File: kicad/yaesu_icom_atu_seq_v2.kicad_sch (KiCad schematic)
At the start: 124 parts, among them J1 ICOM ATU, J10 SERIAL, J11 PGLINK, J12 POWER, J13 Icom ATU, J14 I2C, J15 ALC OUT, J16 SEQ A1-3, J17 SEQ B1-3, J18 SEQ C1-3, J19 SEQ D1-3, J2 STBY, J20 SERIAL, J3 TUNER, J4 POWER, J5 I2C, J6 ALC, J7 STBY, J8 TUNER, J9 PVLINK, SW1 TUNE, U1 PC817, U10 PC817, U11 PC817, U12 PC817, U13 PC817, U14 PC817, U15 PC817, U16 PC817, U17 MAX202CPE, U2 L7805, U3 PC817, U4 PC817, U5 PC817, U6 PC817, U7 PC817, U8 PC817, U9 PC817

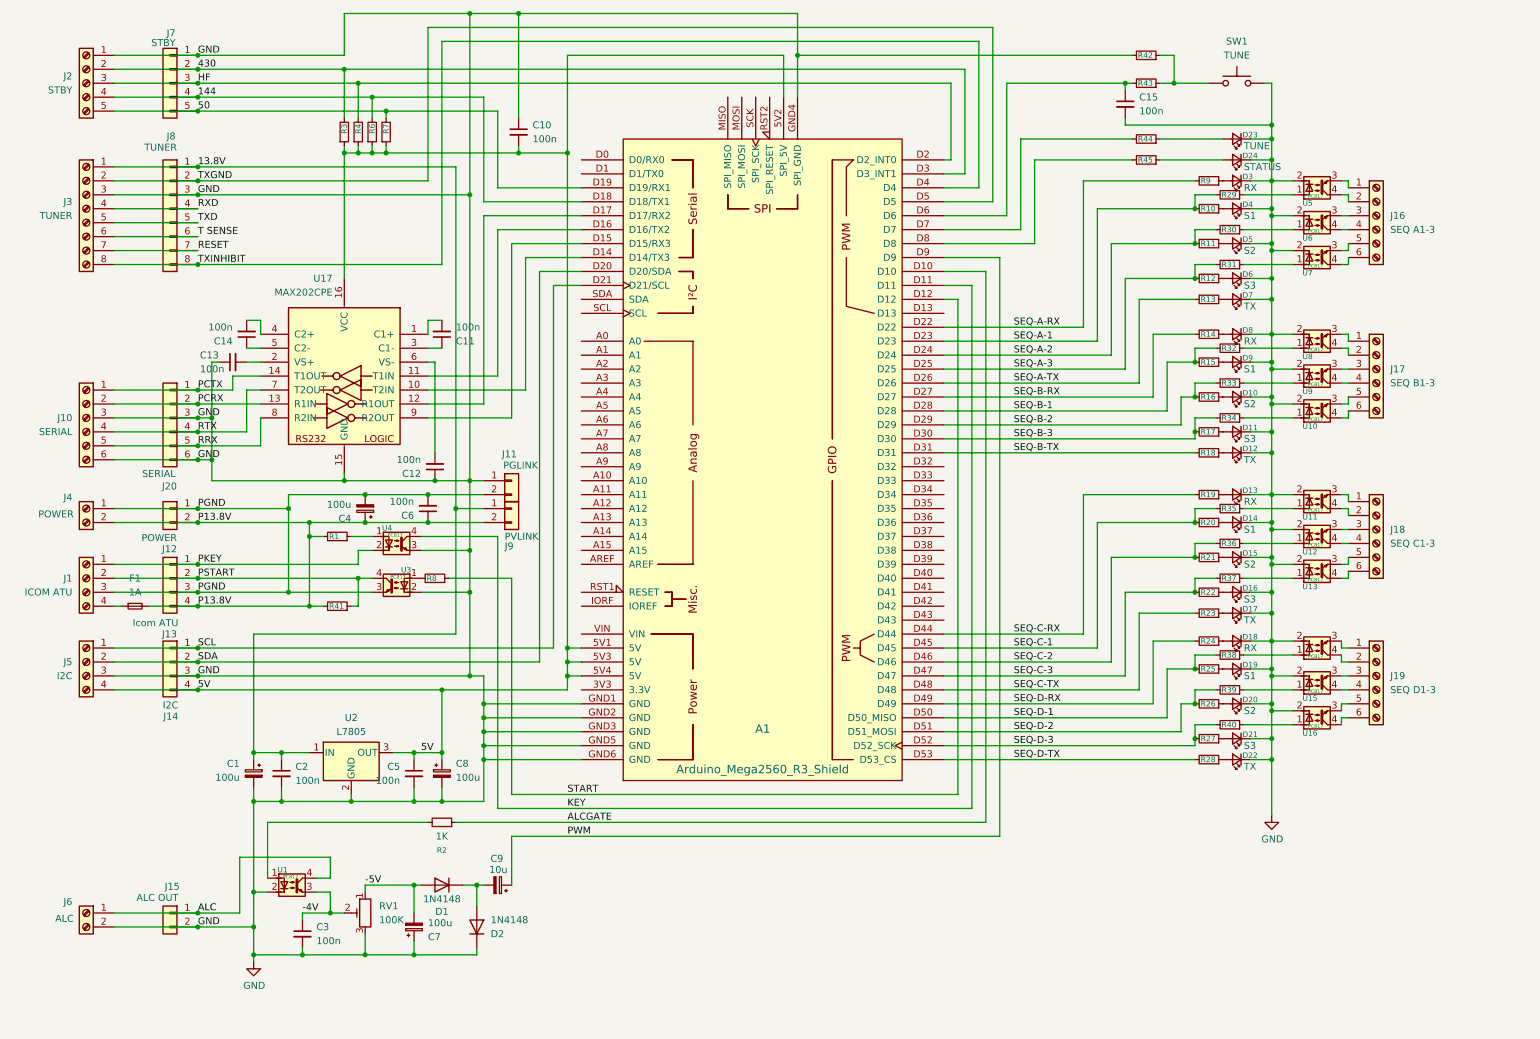
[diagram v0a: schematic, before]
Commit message: update schematic
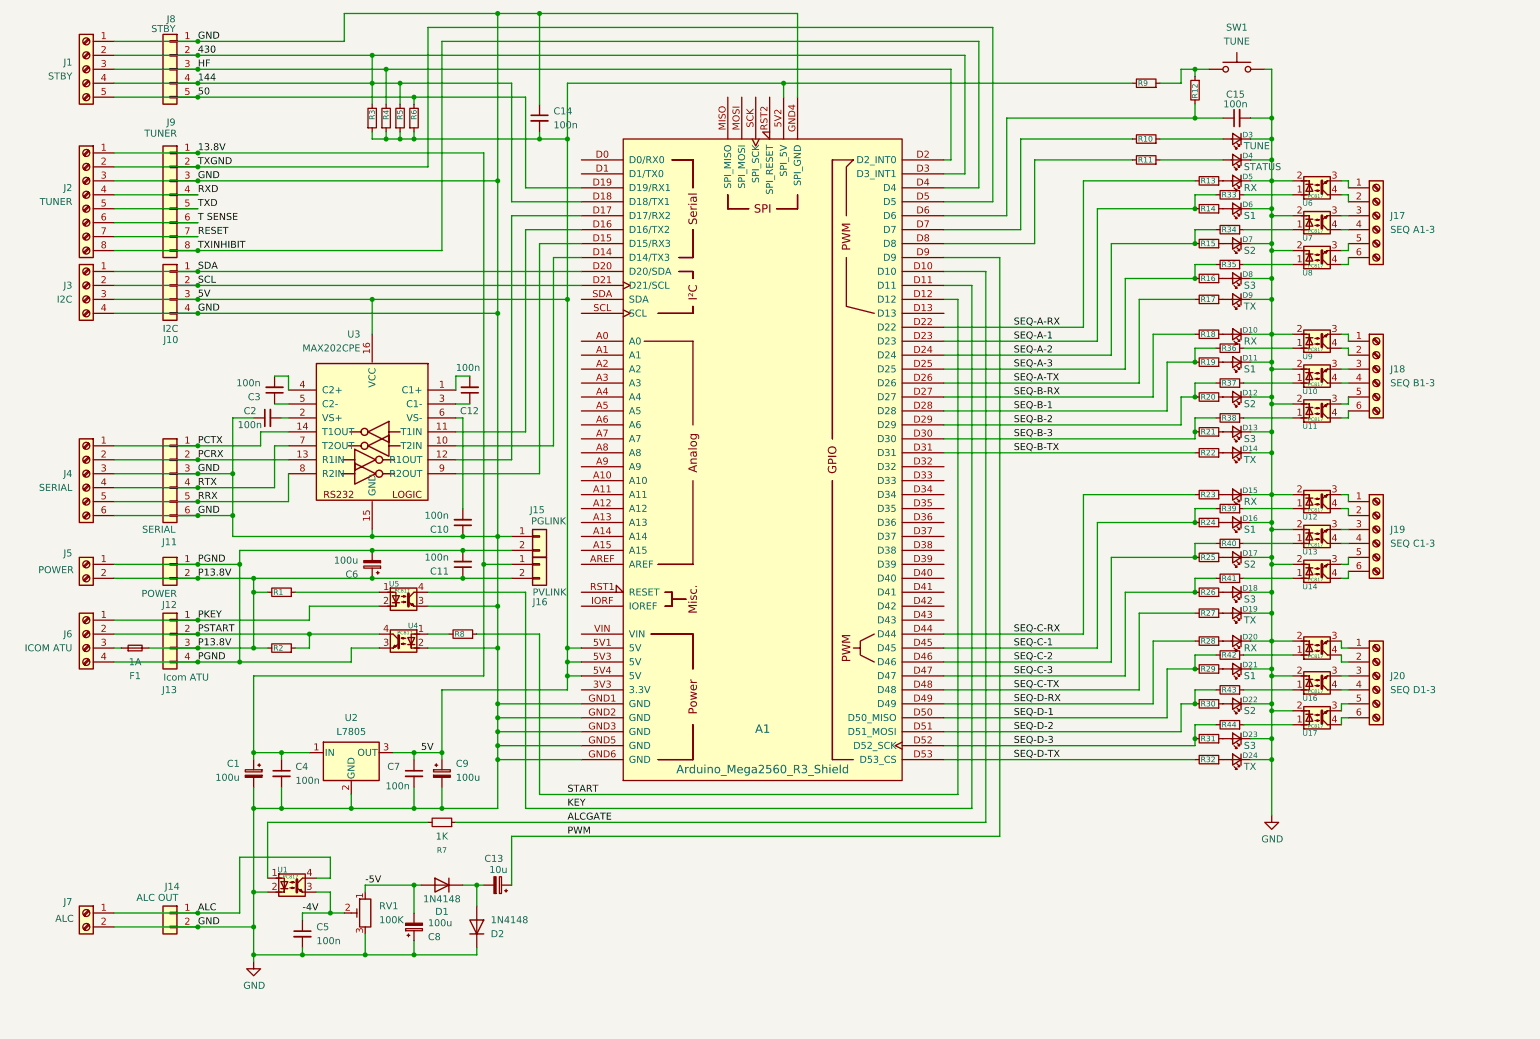
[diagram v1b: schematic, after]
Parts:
- renumbered C12 to C10, C6 to C11, C11 to C12, C9 to C13, C10 to C14, C13 to C2, C14 to C3, C2 to C4, C3 to C5, C4 to C6, C5 to C7, C7 to C8, C8 to C9, D8 to D10, D9 to D11, D10 to D12, D11 to D13, D12 to D14, D13 to D15, D14 to D16, D15 to D17, D16 to D18, D17 to D19, D18 to D20, D19 to D21, D20 to D22, D21 to D23, D22 to D24, D23 to D3, D24 to D4, D3 to D5, D4 to D6, D5 to D7, D6 to D8, D7 to D9, J2 to J1, J14 to J10, J20 to J11, J15 to J14, J11 to J15, J9 to J16, J16 to J17, J17 to J18, J18 to J19, J3 to J2, J19 to J20, J5 to J3, J10 to J4, J4 to J5, J1 to J6, J6 to J7, J7 to J8, J8 to J9, R44 to R10, R45 to R11, R43 to R12, R9 to R13, R10 to R14, R11 to R15, R12 to R16, R13 to R17, R14 to R18, R15 to R19, R41 to R2, R16 to R20, R17 to R21, R18 to R22, R19 to R23, R20 to R24, R21 to R25, R22 to R26, R23 to R27, R24 to R28, R25 to R29, R26 to R30, R27 to R31, R28 to R32, R29 to R33, R30 to R34, R31 to R35, R32 to R36, R33 to R37, R34 to R38, R35 to R39, R36 to R40, R37 to R41, R38 to R42, R39 to R43, R40 to R44, R6 to R5, R7 to R6, R2 to R7, R42 to R9, U9 to U10, U10 to U11, U11 to U12, U12 to U13, U13 to U14, U14 to U15, U15 to U16, U16 to U17, U17 to U3, U3 to U4, U4 to U5, U5 to U6, U6 to U7, U7 to U8, U8 to U9
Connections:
- net 430 is gone; now on net 144: A1.D3 (D3_INT1), J1.2 (Pin_2), J8.2 (Pin_2), R3.2
- net 5V: now also J10.3 (Pin_3), J3.3 (Pin_3), R9.2; no longer J10.4 (Pin_4), J3.4 (Pin_4)
- net GND: now also J10.4 (Pin_4), J3.4 (Pin_4); no longer J10.3 (Pin_3), J3.3 (Pin_3), R9.2
- net P13.8V: now also J13.3 (Pin_3); no longer J13.4 (Pin_4)
- net PGND: now also J13.4 (Pin_4), J6.4 (Pin_4); no longer J13.3 (Pin_3), J6.3 (Pin_3)
- net SCL: now also J10.2 (Pin_2), J3.2 (Pin_2); no longer J10.1 (Pin_1), J3.1 (Pin_1)
- net SDA: now also J10.1 (Pin_1), J3.1 (Pin_1); no longer J10.2 (Pin_2), J3.2 (Pin_2)
- net at F1.1: now also J6.3 (Pin_3); no longer J6.4 (Pin_4)
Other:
- moved on the sheet: C10, C11, C12, C14, C15, C2, C3, C6, F1, J1, J10, J11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

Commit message: Update schematic and PCB
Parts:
- removed D3: TUNE, Custom:LED_THT_L72CB_Kingbright, symbol Device:LED_Small
- removed U1, U10, U11, U12, U13, U14, U15, U16, U17, U4, U5, U6, U7, U8, U9: PC817, Custom:PC817_DIP, symbol Misc_Custom:PC817_small
- added BZ1: Buzzer, Buzzer_Beeper:Buzzer_TDK_PS1240P02BT_D12.2mm_H6.5mm, symbol Device:Buzzer
- added C11, C12, C13, C15, C3, C7, C8, C9: 10n, Capacitor_THT:C_Disc_D4.3mm_W1.9mm_P5.00mm, symbol Device:C_Small
- added C25, C26, C27, C28, C29, C30, C31, C32, C33, C34, C35, C36: 10nF, Capacitor_THT:C_Disc_D5.1mm_W3.2mm_P5.00mm, symbol Custom:C_Smaller
- added C6: 100n, Capacitor_THT:C_Disc_D4.3mm_W1.9mm_P5.00mm, symbol Device:C_Small
- added D1, D2, D28, D29, D30, D31, D32, D33, D34, D35, D36, D37, D38, D39: 1.5KE18A, Diode_THT:D_DO-201AE_P15.24mm_Horizontal, symbol Custom:D_TVS_U_Small
- added D27, D3: 1N4148, Diode_THT:D_DO-35_SOD27_P7.62mm_Horizontal, symbol Diode:1N4148
- added E1: (no value), Custom:Hammond_Enclosure_RM2095L, symbol Custom:Enclosure
- added J10: P13.8V, Connector_PinHeader_2.54mm:PinHeader_2x02_P2.54mm_Vertical, symbol Connector_Generic:Conn_02x02_Counter_Clockwise
- added J11, J19: SPARE, Connector_PinHeader_2.54mm:PinHeader_1x05_P2.54mm_Vertical, symbol Connector_Generic:Conn_01x05
- added J20: RVLINK, Connector_PinHeader_2.54mm:PinHeader_1x02_P2.54mm_Vertical, symbol Connector_Generic:Conn_01x02
- added J23, J24: ANALOG, Connector_PinHeader_2.54mm:PinHeader_1x04_P2.54mm_Vertical, symbol Connector_Generic:Conn_01x04
- added J25: EXP, Connector_PinHeader_2.54mm:PinHeader_1x16_P2.54mm_Vertical, symbol Connector:Conn_01x16_Pin
- added J7: SPARE, TerminalBlock_Phoenix:TerminalBlock_Phoenix_PT-1,5-5-3.5-H_1x05_P3.50mm_Horizontal, symbol Connector:Screw_Terminal_01x05
- added J9: PGND, Connector_PinHeader_2.54mm:PinHeader_2x02_P2.54mm_Vertical, symbol Connector_Generic:Conn_02x02_Counter_Clockwise
- added L1, L2, L3, L4: 100uH, Inductor_THT:L_Axial_L9.5mm_D4.0mm_P5.08mm_Vertical_Fastron_SMCC, symbol Device:L_Small
- added PR1, PR2, PR3, PR4, PR5: (no value), Custom:Prototype Area 5x13 with 4 rails (5x17) 2.54mm Grid, symbol Custom:Prototype_Area
- added Q1: BC547, Package_TO_SOT_THT:TO-92L_Wide, symbol Transistor_BJT:BC547
- added R1, R14, R15, R2, R3, R4, R5, R53, R54, R55, R56, R57, R58, R59, R6, R60, R61, R62, R63, R64: 1K, Resistor_THT:R_Axial_DIN0207_L6.3mm_D2.5mm_P10.16mm_Horizontal, symbol Device:R_Small
- added U1, U4, U5, U6, U7: PC817, Custom:3 x PC817 on a DIP-16_W7.62mm_Socket_LongPads, symbol Misc_Custom:PC817_smallx3
- C1, C2: KiLib_Generator (none) -> capacitor/THT/other
- C10: renamed from C5; KiLib_Generator (none) -> capacitor/THT/other
- C14: renamed from C6; KiLib_Generator (none) -> capacitor/THT/other
- C16: renamed from C7; KiLib_Generator (none) -> capacitor/THT/other
- C17: renamed from C8; value 100u -> 10u; KiLib_Generator (none) -> capacitor/THT/other
- C18: renamed from C9; KiLib_Generator (none) -> capacitor/THT/other
- C19: renamed from C12; KiLib_Generator (none) -> capacitor/THT/other
- C20: renamed from C10; KiLib_Generator (none) -> capacitor/THT/other
- C21: renamed from C11; KiLib_Generator (none) -> capacitor/THT/other
- C22: renamed from C13; value 10u -> 4u7; KiLib_Generator (none) -> capacitor/THT/other
- C23: renamed from C14; KiLib_Generator (none) -> capacitor/THT/other
- C24: renamed from C15; KiLib_Generator (none) -> capacitor/THT/other
- C4: renamed from C3; KiLib_Generator (none) -> capacitor/THT/other
- C5: renamed from C4; KiLib_Generator (none) -> capacitor/THT/other
- D10: renamed from D8; KiLib_Generator (none) -> LED/THT
- D11: renamed from D9; KiLib_Generator (none) -> LED/THT
- D12: renamed from D10; KiLib_Generator (none) -> LED/THT
- D13: renamed from D11; KiLib_Generator (none) -> LED/THT
- D14: renamed from D12; KiLib_Generator (none) -> LED/THT
- D15: renamed from D13; KiLib_Generator (none) -> LED/THT
- D16: renamed from D14; KiLib_Generator (none) -> LED/THT
- D17: renamed from D15; KiLib_Generator (none) -> LED/THT
- D18: renamed from D16; KiLib_Generator (none) -> LED/THT
- D19: renamed from D17; KiLib_Generator (none) -> LED/THT
- D20: renamed from D18; KiLib_Generator (none) -> LED/THT
- D21: renamed from D19; KiLib_Generator (none) -> LED/THT
- D22: renamed from D20; KiLib_Generator (none) -> LED/THT
- D23: renamed from D21; KiLib_Generator (none) -> LED/THT
- D24: renamed from D22; KiLib_Generator (none) -> LED/THT
- D25: renamed from D23; KiLib_Generator (none) -> LED/THT
- D26: renamed from D24; KiLib_Generator (none) -> LED/THT
- D4: renamed from D1; KiLib_Generator (none) -> diode/THT
- D5: renamed from D2; KiLib_Generator (none) -> diode/THT
- D6: renamed from D4; KiLib_Generator (none) -> LED/THT
- D7: renamed from D5; KiLib_Generator (none) -> LED/THT
- D8: renamed from D6; KiLib_Generator (none) -> LED/THT
- D9: renamed from D7; KiLib_Generator (none) -> LED/THT
- J1, J2, J3, J4, J5, J6: KiLib_Generator (none) -> terminal_block/Phoenix
- J12: renamed from J8; KiLib_Generator (none) -> connector/pin_header_socket
- J13: renamed from J9; KiLib_Generator (none) -> connector/pin_header_socket
- J14: renamed from J10; KiLib_Generator (none) -> connector/pin_header_socket
- J15: renamed from J11; KiLib_Generator (none) -> connector/pin_header_socket
- J16: renamed from J12; KiLib_Generator (none) -> connector/pin_header_socket
- J17: renamed from J13; KiLib_Generator (none) -> connector/pin_header_socket
- J18: renamed from J14; KiLib_Generator (none) -> connector/pin_header_socket
- J21: renamed from J15; KiLib_Generator (none) -> connector/pin_header_socket
- J22: renamed from J16; KiLib_Generator (none) -> connector/pin_header_socket
- J26: renamed from J17; KiLib_Generator (none) -> terminal_block/Phoenix
- J27: renamed from J18; KiLib_Generator (none) -> terminal_block/Phoenix
- J28: renamed from J19; KiLib_Generator (none) -> terminal_block/Phoenix
- J29: renamed from J20; KiLib_Generator (none) -> terminal_block/Phoenix
- J8: renamed from J7; KiLib_Generator (none) -> terminal_block/Phoenix
- R10: renamed from R4; KiLib_Generator (none) -> resistor/THT
- R11: renamed from R5; KiLib_Generator (none) -> resistor/THT
- R12: renamed from R6; KiLib_Generator (none) -> resistor/THT
- R13: renamed from R7; value 1K -> 470R; KiLib_Generator (none) -> resistor/THT
- R16: renamed from R8; KiLib_Generator (none) -> resistor/THT
- R17: renamed from R9; KiLib_Generator (none) -> resistor/THT
- R18: renamed from R10; value 1K -> 390R; KiLib_Generator (none) -> resistor/THT
- R19: renamed from R11; KiLib_Generator (none) -> resistor/THT
- R20: renamed from R12; KiLib_Generator (none) -> resistor/THT
- R21: renamed from R13; KiLib_Generator (none) -> resistor/THT
- R22: renamed from R14; KiLib_Generator (none) -> resistor/THT
- R23: renamed from R15; KiLib_Generator (none) -> resistor/THT
- R24: renamed from R16; KiLib_Generator (none) -> resistor/THT
- R25: renamed from R17; KiLib_Generator (none) -> resistor/THT
- R26: renamed from R18; KiLib_Generator (none) -> resistor/THT
- R27: renamed from R19; KiLib_Generator (none) -> resistor/THT
- R28: renamed from R20; KiLib_Generator (none) -> resistor/THT
- R29: renamed from R21; KiLib_Generator (none) -> resistor/THT
- R30: renamed from R22; KiLib_Generator (none) -> resistor/THT
- R31: renamed from R23; KiLib_Generator (none) -> resistor/THT
- R32: renamed from R24; KiLib_Generator (none) -> resistor/THT
- R33: renamed from R25; KiLib_Generator (none) -> resistor/THT
- R34: renamed from R26; KiLib_Generator (none) -> resistor/THT
- R35: renamed from R27; KiLib_Generator (none) -> resistor/THT
- R36: renamed from R28; KiLib_Generator (none) -> resistor/THT
- R37: renamed from R29; KiLib_Generator (none) -> resistor/THT
- R38: renamed from R30; KiLib_Generator (none) -> resistor/THT
- R39: renamed from R31; KiLib_Generator (none) -> resistor/THT
- R40: renamed from R32; KiLib_Generator (none) -> resistor/THT
- R41: renamed from R33; KiLib_Generator (none) -> resistor/THT
- R42: renamed from R34; KiLib_Generator (none) -> resistor/THT
- R43: renamed from R35; KiLib_Generator (none) -> resistor/THT
- R44: renamed from R36; KiLib_Generator (none) -> resistor/THT
- R45: renamed from R37; KiLib_Generator (none) -> resistor/THT
- R46: renamed from R38; KiLib_Generator (none) -> resistor/THT
- R47: renamed from R39; KiLib_Generator (none) -> resistor/THT
- R48: renamed from R40; KiLib_Generator (none) -> resistor/THT
- R49: renamed from R41; KiLib_Generator (none) -> resistor/THT
- R50: renamed from R42; KiLib_Generator (none) -> resistor/THT
- R51: renamed from R43; KiLib_Generator (none) -> resistor/THT
- R52: renamed from R44; KiLib_Generator (none) -> resistor/THT
- R7: renamed from R1; KiLib_Generator (none) -> resistor/THT
- R8: renamed from R2; KiLib_Generator (none) -> resistor/THT
- R9: renamed from R3; KiLib_Generator (none) -> resistor/THT
- SW1: footprint Package_DIP:DIP-24_W7.62mm -> Button_Switch_THT:SW_PUSH-12mm
- U2: KiLib_Generator (none) -> package/TO_SOT/THT
- U3: footprint (none) -> Package_DIP:DIP-16_W7.62mm_Socket_LongPads; KiLib_Generator (none) -> package/DIP/legacy
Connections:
- net -4V: now also U1.9
- net 13.8V: now also J20.2 (Pin_2), J25.1 (Pin_1), PR1.3 (VDD), PR2.3 (VDD), PR3.3 (VDD), PR4.3 (VDD), PR5.3 (VDD), R14.1; no longer J13.1 (Pin_1), J2.1 (Pin_1)
- net 144: now also R3.2; no longer A1.D18 (D18/TX1), A1.D3 (D3_INT1), J1.2 (Pin_2), J12.2 (Pin_2), R11.2, R9.2
- net 50: now also R4.2; no longer A1.D19 (D19/RX1), R12.2
- net 5V: now also J25.2 (Pin_2), PR1.2 (VCC), PR2.2 (VCC), PR3.2 (VCC), PR4.2 (VCC), PR5.2 (VCC)
- net ALC: now also C6.1, U1.10
- net GND: now also BZ1.2 (-), C12.2, C13.2, C3.2, C6.2, C7.2, C8.2, C9.1, D27.2 (A), J25.3 (Pin_3), PR1.1 (GND), PR1.4 (GND), PR2.1 (GND), PR2.4 (GND), PR3.1 (GND), PR3.4 (GND), PR4.1 (GND), PR4.4 (GND), PR5.1 (GND), PR5.4 (GND), Q1.3 (E), U1.15, U1.5, U1.8, U4.2, U4.5, U4.8, U5.2, U5.5, U5.8, U6.2, U6.5, U6.8, U7.2, U7.5, U7.8
- net HF: now also R2.2; no longer A1.D2 (D2_INT0), R10.2
- net KEY: now also U1.16
- net P13.8V: now also J10.1 (Pin_1), J10.2 (Pin_2), J10.3 (Pin_3), J10.4 (Pin_4); no longer J17.3 (Pin_3)
- net PGND: now also C11.2, C15.2, D1.2 (A2), D2.2 (A2), J9.1 (Pin_1), J9.2 (Pin_2), J9.3 (Pin_3), J9.4 (Pin_4), U1.12
- net PKEY: now also D2.1 (A1), L2.1
- net PSTART: now also D1.1 (A1), L1.1; no longer R8.1
- net PWM: now also R15.1; no longer C22.1
- net SEQ-A-1: now also A1.D35; no longer A1.D23
- net SEQ-A-2: now also A1.D36; no longer A1.D24
- net SEQ-A-3: now also A1.D37; no longer A1.D25
- net SEQ-A-RX: now also A1.D34; no longer A1.D22
- net SEQ-A-TX: now also A1.D38; no longer A1.D26
- net SEQ-B-1: now also A1.D40; no longer A1.D28
- net SEQ-B-2: now also A1.D41; no longer A1.D29
- net SEQ-B-3: now also A1.D42; no longer A1.D30
- net SEQ-B-RX: now also A1.D39; no longer A1.D27
- net SEQ-B-TX: now also A1.D43; no longer A1.D31
- net START: now also R16.2, U1.4; no longer A1.D12, R16.1
- net TXGND: now also R5.2; no longer A1.D5
- net TXINHIBIT: now also R6.2; no longer A1.D4
- net at R45.1: now also U5.4
- net at J27.3 (Pin_3): now also C29.2, D29.1 (A1), R57.1
- net at J27.4 (Pin_4): now also C29.1, D29.2 (A2), U5.12
- net ND18: now reaches D18.2 (A), R32.1
- net ND18: now also U6.11, U6.6
- net at R7.1: now also U1.1
- net at A1.A12: now also J24.1 (Pin_1)
- net at A1.A13: now also J24.2 (Pin_2)
- net at A1.A14: now also J24.3 (Pin_3)
- net at A1.A15: now also J24.4 (Pin_4)
- net at A1.A4: now also J23.1 (Pin_1)
- net at A1.A5: now also J23.2 (Pin_2)
- net at A1.A6: now also J23.3 (Pin_3)
- net at A1.A7: now also J23.4 (Pin_4)
- net D13: now reaches A1.D13
- net D13: now also J25.4 (Pin_4)
- net D32: now reaches A1.D32
- net D32: now also J25.15 (Pin_15)
- net D33: now reaches A1.D33
- net D33: now also J25.16 (Pin_16)
- net at A1.D6, C24.1: now also R20.1; no longer R20.2
- net at R46.1: now also U5.1
- net at J26.1 (Pin_1): now also C25.2, D31.1 (A1), R53.1
- net at J26.2 (Pin_2): now also C25.1, D31.2 (A2), U4.9
- net at J26.3 (Pin_3): now also C26.2, D32.1 (A1), R54.1
- net at J26.4 (Pin_4): now also C26.1, D32.2 (A2), U4.12
- net at J26.5 (Pin_5): now also C27.2, D33.1 (A1), R55.1
- net at J26.6 (Pin_6): now also C27.1, D33.2 (A2), U4.15
- net at R13.2: now also U1.7
- net at R41.1: now also U4.7
- net ND14: now reaches D14.2 (A), R28.1
- net ND14: now also U5.14, U5.3
- net at R50.1: now also U7.7
- net at R52.1: now also U7.1
- net at J29.5 (Pin_5): now also C36.2, D39.1 (A1), R64.1
- net at J29.6 (Pin_6): now also C36.1, D39.2 (A2), U7.15
- net at R51.1: now also U7.4
- net at J29.3 (Pin_3): now also C35.2, D38.1 (A1), R63.1
- net at J29.4 (Pin_4): now also C35.1, D38.2 (A2), U7.12
- net at R47.1: now also U6.7
- net at R42.1: now also U4.4
- net at R44.1: now also U5.7
- net ND9: now reaches D9.2 (A), R23.1
- net ND9: now also U4.14, U4.3
- net at R48.1: now also U6.4
- net at J28.3 (Pin_3): now also C32.2, D35.1 (A1), R60.1
- net at J28.4 (Pin_4): now also C32.1, D35.2 (A2), U6.12
- net ND23: now reaches D23.2 (A), R37.1
- net ND23: now also U7.11, U7.6
- net ND19: now reaches D19.2 (A), R33.1
- net ND19: now also U6.14, U6.3
- net at J29.1 (Pin_1): now also C34.2, D37.1 (A1), R62.1
- net at J29.2 (Pin_2): now also C34.1, D37.2 (A2), U7.9
- net at R18.1: now also BZ1.1 (+), D27.1 (K)
- net at J28.1 (Pin_1): now also C31.2, D34.1 (A1), R59.1
- net at J28.2 (Pin_2): now also C31.1, D34.2 (A2), U6.9
- net ND24: now reaches D24.2 (A), R38.1
- net ND24: now also U7.14, U7.3
- net ND8: now reaches D8.2 (A), R22.1
- net ND8: now also U4.11, U4.6
- net at J28.5 (Pin_5): now also C33.2, D36.1 (A1), R61.1
- net at J28.6 (Pin_6): now also C33.1, D36.2 (A2), U6.15
- net at J27.1 (Pin_1): now also C28.2, D28.1 (A1), R56.1
- net at J27.2 (Pin_2): now also C28.1, D28.2 (A2), U5.9
- net at J27.5 (Pin_5): now also C30.2, D30.1 (A1), R58.1
- net at J27.6 (Pin_6): now also C30.1, D30.2 (A2), U5.15
- net at F1.1, J6.3 (Pin_3): now also J17.3 (Pin_3)
- net at R17.1, SW1.1: now also R20.2; no longer R20.1
- net at R43.1: now also U4.1
- net at R49.1: now also U6.1
- net ND13: now reaches D13.2 (A), R27.1
- net ND13: now also U5.11, U5.6
- net -5V renamed -12V
- new net: R55.2, U4.16
- new net: C15.1, L2.2, L4.2
- new net: R54.2, U4.13
- new net: A1.D12, R16.1
- new net: A1.D18 (D18/TX1), C12.1, R11.2, R3.1
- new net: A1.D19 (D19/RX1), C13.1, R12.2, R4.1
- new net: A1.D2 (D2_INT0), C7.1, R10.2, R2.1
- new net: A1.D3 (D3_INT1), C3.1, R1.1, R9.2
- new net: A1.D4, C9.2, R6.1
- new net: A1.D5, C8.1, R5.1
- new net: R56.2, U5.10
- new net: R53.2, U4.10
- new net: C22.1, Q1.1 (C), R14.2
- new net: R61.2, U6.16
- new net: J11.1 (Pin_1), J19.1 (Pin_1), J7.1 (Pin_1)
- new net: J11.2 (Pin_2), J19.2 (Pin_2), J7.2 (Pin_2)
- new net: J11.3 (Pin_3), J19.3 (Pin_3), J7.3 (Pin_3)
- new net: J11.4 (Pin_4), J19.4 (Pin_4), J7.4 (Pin_4)
- new net: J11.5 (Pin_5), J19.5 (Pin_5), J7.5 (Pin_5)
- new net: R63.2, U7.13
- new net: R64.2, U7.16
- new net: R57.2, U5.13
- new net: L4.1, U1.2
- new net: R62.2, U7.10
- new net: D3.2 (A), L3.1
- new net: C11.1, L1.2, L3.2, R8.1
- new net: R60.2, U6.13
- new net: R58.2, U5.16
- new net: Q1.2 (B), R15.2
- new net: D3.1 (K), U1.13
- new net: R59.2, U6.10
- new net 430: J1.2 (Pin_2), J12.2 (Pin_2), R1.2
- new net D22: A1.D22, J25.5 (Pin_5)
- new net D23: A1.D23, J25.6 (Pin_6)
- new net D24: A1.D24, J25.7 (Pin_7)
- new net D25: A1.D25, J25.8 (Pin_8)
- new net D26: A1.D26, J25.9 (Pin_9)
- new net D27: A1.D27, J25.10 (Pin_10)
- new net D28: A1.D28, J25.11 (Pin_11)
- new net D29: A1.D29, J25.12 (Pin_12)
- new net D30: A1.D30, J25.13 (Pin_13)
- new net D31: A1.D31, J25.14 (Pin_14)
- new net R13.8V: J13.1 (Pin_1), J2.1 (Pin_1), J20.1 (Pin_1)
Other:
- moved on the sheet: C1, C19, C2, C20, C24, C4, C5, D10, D11, D12, D13, D14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

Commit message: Update schematic and PCB
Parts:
- J25: symbol Connector:Conn_01x16_Pin -> Connector_Generic:Conn_01x16
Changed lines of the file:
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@@
 	)
 	(symbol
-		(lib_id "Connector:Conn_01x16_Pin")
+		(lib_id "Connector_Generic:Conn_01x16")
 		(at 203.2 78.74 0)
-		(mirror y)
 		(unit 1)
 		(body_style 1)
@@
 		(dnp no)
 		(property "Reference" "J25"
-			(at 200.66 56.642 0)
+			(at 202.946 56.642 0)
 			(show_name no)
 			(do_not_autoplace no)
@@
 		)
 		(property "Value" "EXP"
-			(at 200.914 58.42 0)
+			(at 203.2 58.42 0)
 			(show_name no)
 			(do_not_autoplace no)

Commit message: Update schematic and PCB with ALC 10 turn pot
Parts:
- RV1: value 100K -> 47K; footprint Potentiometer_THT:Potentiometer_Runtron_RM-065_Vertical -> Potentiometer_THT:Potentiometer_Bourns_3296W_Vertical
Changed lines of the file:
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@@
 			)
 		)
-		(property "Value" "100K"
+		(property "Value" "47K"
 			(at 76.2 179.0699 0)
 			(show_name no)
@@
 			)
 		)
-		(property "Footprint" "Potentiometer_THT:Potentiometer_Runtron_RM-065_Vertical"
+		(property "Footprint" "Potentiometer_THT:Potentiometer_Bourns_3296W_Vertical"
 			(at 73.66 177.8 0)
 			(hide yes)
